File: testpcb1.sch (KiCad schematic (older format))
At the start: 42 parts

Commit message: pinout pro micro
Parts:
- added RV?: R_POT, symbol Device:R_POT
- added SW?: Rotary_Encoder, symbol Device:Rotary_Encoder
- added SW?: SW_Push, symbol Switch:SW_Push
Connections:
- net col0: now also U?.15 (14/PB3)
- net col1: now also U?.14 (16/PB2)
- net col2: now also U?.13 (10/PB6)
- net col3: now also U?.1 (TX0/PD3)
- net row0: now also U?.20 (A3/PF4)
- net row1: now also U?.19 (A2/PF5)
- net row2: now also U?.18 (A1/PF6)
- net row3: now also U?.17 (A0/PF7)
- net row4: now reaches U?.16 (15/PB1)
- net VCC: now reaches U?.21 (VCC)
- net RST: now reaches U?.22 (RST)
- net RST: now also SW?.1
- net GND: now reaches U?.23 (GND)
- net GND: now also SW?.2
- net POT: now reaches U?.7 (4/PD4)
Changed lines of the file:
@@
 Text GLabel 1150 1600 0    31   Input ~ 0
 SDL
+$Comp
+L Device:Rotary_Encoder SW?
+U 1 1 5F279AE0
+P 8850 1500
+F 0 "SW?" H 9080 1546 50  0000 L CNN
+F 1 "Rotary_Encoder" H 9080 1455 50  0000 L CNN
+F 2 "" H 8700 1660 50  0001 C CNN
+F 3 "~" H 8850 1760 50  0001 C CNN
+	1    8850 1500
+	1    0    0    -1
+$EndComp
+$Comp
+L Device:R_POT RV?
+U 1 1 5F27C616
+P 9000 4000
+F 0 "RV?" H 8931 4046 50  0000 R CNN
+F 1 "R_POT" H 8931 3955 50  0000 R CNN
+F 2 "" H 9000 4000 50  0001 C CNN
+F 3 "~" H 9000 4000 50  0001 C CNN
+	1    9000 4000
+	1    0    0    -1
+$EndComp
+Wire Wire Line
+	1300 1700 1150 1700
+Text GLabel 1150 1700 0    31   Input ~ 0
+POT
+Text GLabel 2850 1300 2    31   Input ~ 0
+RST
+Wire Wire Line
+	2700 1300 2850 1300
+Wire Wire Line
+	2700 1200 2850 1200
+Text GLabel 2850 1200 2    31   Input ~ 0
+GND
+$Comp
+L Switch:SW_Push SW?
+U 1 1 5F289AFB
+P 4200 1500
+F 0 "SW?" H 4200 1785 50  0000 C CNN
+F 1 "SW_Push" H 4200 1694 50  0000 C CNN
+F 2 "" H 4200 1700 50  0001 C CNN
+F 3 "~" H 4200 1700 50  0001 C CNN
+	1    4200 1500
+	1    0    0    -1
+$EndComp
+Wire Wire Line
+	4400 1500 4800 1500
+Wire Wire Line
+	4000 1500 3500 1500
+Text GLabel 3500 1500 0    31   Input ~ 0
+RST
+Text GLabel 4800 1500 2    31   Input ~ 0
+GND
+Text GLabel 2850 1400 2    31   Input ~ 0
+VCC
+Wire Wire Line
+	2850 1400 2700 1400
+Text GLabel 2850 1500 2    31   Input ~ 0
+row0
+Text GLabel 2850 1600 2    31   Input ~ 0
+row1
+Text GLabel 2850 1700 2    31   Input ~ 0
+row2
+Text GLabel 2850 1800 2    31   Input ~ 0
+row3
+Text GLabel 2850 1900 2    31   Input ~ 0
+row4
+Wire Wire Line
+	2850 1500 2700 1500
+Wire Wire Line
+	2700 1600 2850 1600
+Wire Wire Line
+	2850 1700 2700 1700
+Wire Wire Line
+	2700 1800 2850 1800
+Wire Wire Line
+	2850 1900 2700 1900
+Text GLabel 2850 2000 2    31   Input ~ 0
+col0
+Text GLabel 2850 2100 2    31   Input ~ 0
+col1
+Text GLabel 2850 2200 2    31   Input ~ 0
+col2
+Text GLabel 1150 1100 0    31   Input ~ 0
+col3
+Wire Wire Line
+	2850 2000 2700 2000
+Wire Wire Line
+	2700 2100 2850 2100
+Wire Wire Line
+	2850 2200 2700 2200
+Wire Wire Line
+	1300 1100 1150 1100
 $EndSCHEMATC

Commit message: vcc and gnd
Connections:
- net GND: no longer U?.23 (GND)
- net col3: now also U?.12 (9/PB5); no longer U?.1 (TX0/PD3)
- net ROT2: now reaches U?.2 (RX1/PD2)
- net VCC: no longer names the net of U?.21 (VCC)
- new net ROT1: U?.1 (TX0/PD3)
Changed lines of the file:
@@
 Wire Wire Line
 	2700 1200 2850 1200
-Text GLabel 2850 1200 2    31   Input ~ 0
-GND
 $Comp
 L Switch:SW_Push SW?
@@
 Text GLabel 4800 1500 2    31   Input ~ 0
 GND
-Text GLabel 2850 1400 2    31   Input ~ 0
-VCC
 Wire Wire Line
 	2850 1400 2700 1400
@@
 Text GLabel 2850 2200 2    31   Input ~ 0
 col2
-Text GLabel 1150 1100 0    31   Input ~ 0
+Text GLabel 1150 2200 0    31   Input ~ 0
 col3
 Wire Wire Line
@@
 	2850 2200 2700 2200
 Wire Wire Line
+	1300 2200 1150 2200
+Wire Wire Line
 	1300 1100 1150 1100
+Text GLabel 1150 1100 0    31   Input ~ 0
+ROT1
+Wire Wire Line
+	1300 1200 1150 1200
+Text GLabel 1150 1200 0    31   Input ~ 0
+ROT2
 $EndSCHEMATC

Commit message: power symbol library
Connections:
- net GND: now also U?.23 (GND)
- net VCC: now reaches U?.21 (VCC)
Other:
- moved on the sheet: SW?
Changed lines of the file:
@@
 Wire Wire Line
 	2700 1300 2850 1300
-Wire Wire Line
-	2700 1200 2850 1200
 $Comp
 L Switch:SW_Push SW?
 U 1 1 5F289AFB
-P 4200 1500
-F 0 "SW?" H 4200 1785 50  0000 C CNN
-F 1 "SW_Push" H 4200 1694 50  0000 C CNN
-F 2 "" H 4200 1700 50  0001 C CNN
-F 3 "~" H 4200 1700 50  0001 C CNN
-	1    4200 1500
+P 4050 1200
+F 0 "SW?" H 4050 1485 50  0000 C CNN
+F 1 "SW_Push" H 4050 1394 50  0000 C CNN
+F 2 "" H 4050 1400 50  0001 C CNN
+F 3 "~" H 4050 1400 50  0001 C CNN
+	1    4050 1200
 	1    0    0    -1
 $EndComp
-Wire Wire Line
-	4400 1500 4800 1500
-Wire Wire Line
-	4000 1500 3500 1500
-Text GLabel 3500 1500 0    31   Input ~ 0
+Text GLabel 3700 1200 0    31   Input ~ 0
 RST
-Text GLabel 4800 1500 2    31   Input ~ 0
-GND
-Wire Wire Line
-	2850 1400 2700 1400
 Text GLabel 2850 1500 2    31   Input ~ 0
 row0
@@
 Text GLabel 1150 1200 0    31   Input ~ 0
 ROT2
+$Comp
+L power:GND #PWR?
+U 1 1 5F27AF68
+P 2800 1200
+F 0 "#PWR?" H 2800 950 50  0001 C CNN
+F 1 "GND" V 2805 1072 50  0000 R CNN
+F 2 "" H 2800 1200 50  0001 C CNN
+F 3 "" H 2800 1200 50  0001 C CNN
+	1    2800 1200
+	0    -1   -1   0
+$EndComp
+$Comp
+L power:VCC #PWR?
+U 1 1 5F27BB79
+P 2800 1400
+F 0 "#PWR?" H 2800 1250 50  0001 C CNN
+F 1 "VCC" V 2815 1528 50  0000 L CNN
+F 2 "" H 2800 1400 50  0001 C CNN
+F 3 "" H 2800 1400 50  0001 C CNN
+	1    2800 1400
+	0    1    1    0
+$EndComp
+Wire Wire Line
+	2800 1200 2700 1200
+Wire Wire Line
+	2700 1400 2800 1400
+$Comp
+L power:GND #PWR?
+U 1 1 5F2859D6
+P 4400 1200
+F 0 "#PWR?" H 4400 950 50  0001 C CNN
+F 1 "GND" V 4405 1072 50  0000 R CNN
+F 2 "" H 4400 1200 50  0001 C CNN
+F 3 "" H 4400 1200 50  0001 C CNN
+	1    4400 1200
+	0    -1   -1   0
+$EndComp
+Wire Wire Line
+	3850 1200 3700 1200
+Wire Wire Line
+	4400 1200 4250 1200
 $EndSCHEMATC

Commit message: OLED
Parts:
- added J?: Conn_01x04_Female, symbol Connector:Conn_01x04_Female
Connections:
- net GND: now also U?.3 (GND), U?.4 (GND), J?.4 (Pin_4)
- net SDA: now also J?.1 (Pin_1)
- net VCC: now also J?.3 (Pin_3)
- net SDL renamed SCL
- net SCL: now also J?.2 (Pin_2)
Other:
- moved on the sheet: RV?, SW?
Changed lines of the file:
@@
 SDA
 Text GLabel 1150 1600 0    31   Input ~ 0
-SDL
+SCL
 $Comp
 L Device:Rotary_Encoder SW?
 U 1 1 5F279AE0
-P 8850 1500
-F 0 "SW?" H 9080 1546 50  0000 L CNN
-F 1 "Rotary_Encoder" H 9080 1455 50  0000 L CNN
-F 2 "" H 8700 1660 50  0001 C CNN
-F 3 "~" H 8850 1760 50  0001 C CNN
-	1    8850 1500
+P 1750 4750
+F 0 "SW?" H 1980 4796 50  0000 L CNN
+F 1 "Rotary_Encoder" H 1980 4705 50  0000 L CNN
+F 2 "" H 1600 4910 50  0001 C CNN
+F 3 "~" H 1750 5010 50  0001 C CNN
+	1    1750 4750
 	1    0    0    -1
 $EndComp
@@
 L Device:R_POT RV?
 U 1 1 5F27C616
-P 9000 4000
-F 0 "RV?" H 8931 4046 50  0000 R CNN
-F 1 "R_POT" H 8931 3955 50  0000 R CNN
-F 2 "" H 9000 4000 50  0001 C CNN
-F 3 "~" H 9000 4000 50  0001 C CNN
-	1    9000 4000
+P 1750 5850
+F 0 "RV?" H 1681 5896 50  0000 R CNN
+F 1 "R_POT" H 1681 5805 50  0000 R CNN
+F 2 "" H 1750 5850 50  0001 C CNN
+F 3 "~" H 1750 5850 50  0001 C CNN
+	1    1750 5850
 	1    0    0    -1
 $EndComp
@@
 Wire Wire Line
 	4400 1200 4250 1200
+$Comp
+L Connector:Conn_01x04_Female J?
+U 1 1 5F2A1EA2
+P 1700 6600
+F 0 "J?" H 1728 6576 50  0000 L CNN
+F 1 "Conn_01x04_Female" H 1728 6485 50  0000 L CNN
+F 2 "" H 1700 6600 50  0001 C CNN
+F 3 "~" H 1700 6600 50  0001 C CNN
+	1    1700 6600
+	1    0    0    -1
+$EndComp
+Text GLabel 1350 6600 0    50   Input ~ 0
+SCL
+Text GLabel 1350 6500 0    50   Input ~ 0
+SDA
+Wire Wire Line
+	1350 6500 1500 6500
+Wire Wire Line
+	1350 6600 1500 6600
+$Comp
+L power:GND #PWR?
+U 1 1 5F2B8AC8
+P 1400 6800
+F 0 "#PWR?" H 1400 6550 50  0001 C CNN
+F 1 "GND" V 1405 6672 50  0000 R CNN
+F 2 "" H 1400 6800 50  0001 C CNN
+F 3 "" H 1400 6800 50  0001 C CNN
+	1    1400 6800
+	0    1    1    0
+$EndComp
+$Comp
+L power:VCC #PWR?
+U 1 1 5F2B9324
+P 1400 6700
+F 0 "#PWR?" H 1400 6550 50  0001 C CNN
+F 1 "VCC" V 1415 6827 50  0000 L CNN
+F 2 "" H 1400 6700 50  0001 C CNN
+F 3 "" H 1400 6700 50  0001 C CNN
+	1    1400 6700
+	0    -1   -1   0
+$EndComp
+Wire Wire Line
+	1400 6700 1500 6700
+Wire Wire Line
+	1500 6800 1400 6800
+$Comp
+L power:GND #PWR?
+U 1 1 5F2BFDF9
+P 1150 1300
+F 0 "#PWR?" H 1150 1050 50  0001 C CNN
+F 1 "GND" V 1155 1172 50  0000 R CNN
+F 2 "" H 1150 1300 50  0001 C CNN
+F 3 "" H 1150 1300 50  0001 C CNN
+	1    1150 1300
+	0    1    1    0
+$EndComp
+Wire Wire Line
+	1300 1300 1200 1300
+Wire Wire Line
+	1300 1400 1200 1400
+Wire Wire Line
+	1200 1400 1200 1300
+Connection ~ 1200 1300
+Wire Wire Line
+	1200 1300 1150 1300
 $EndSCHEMATC

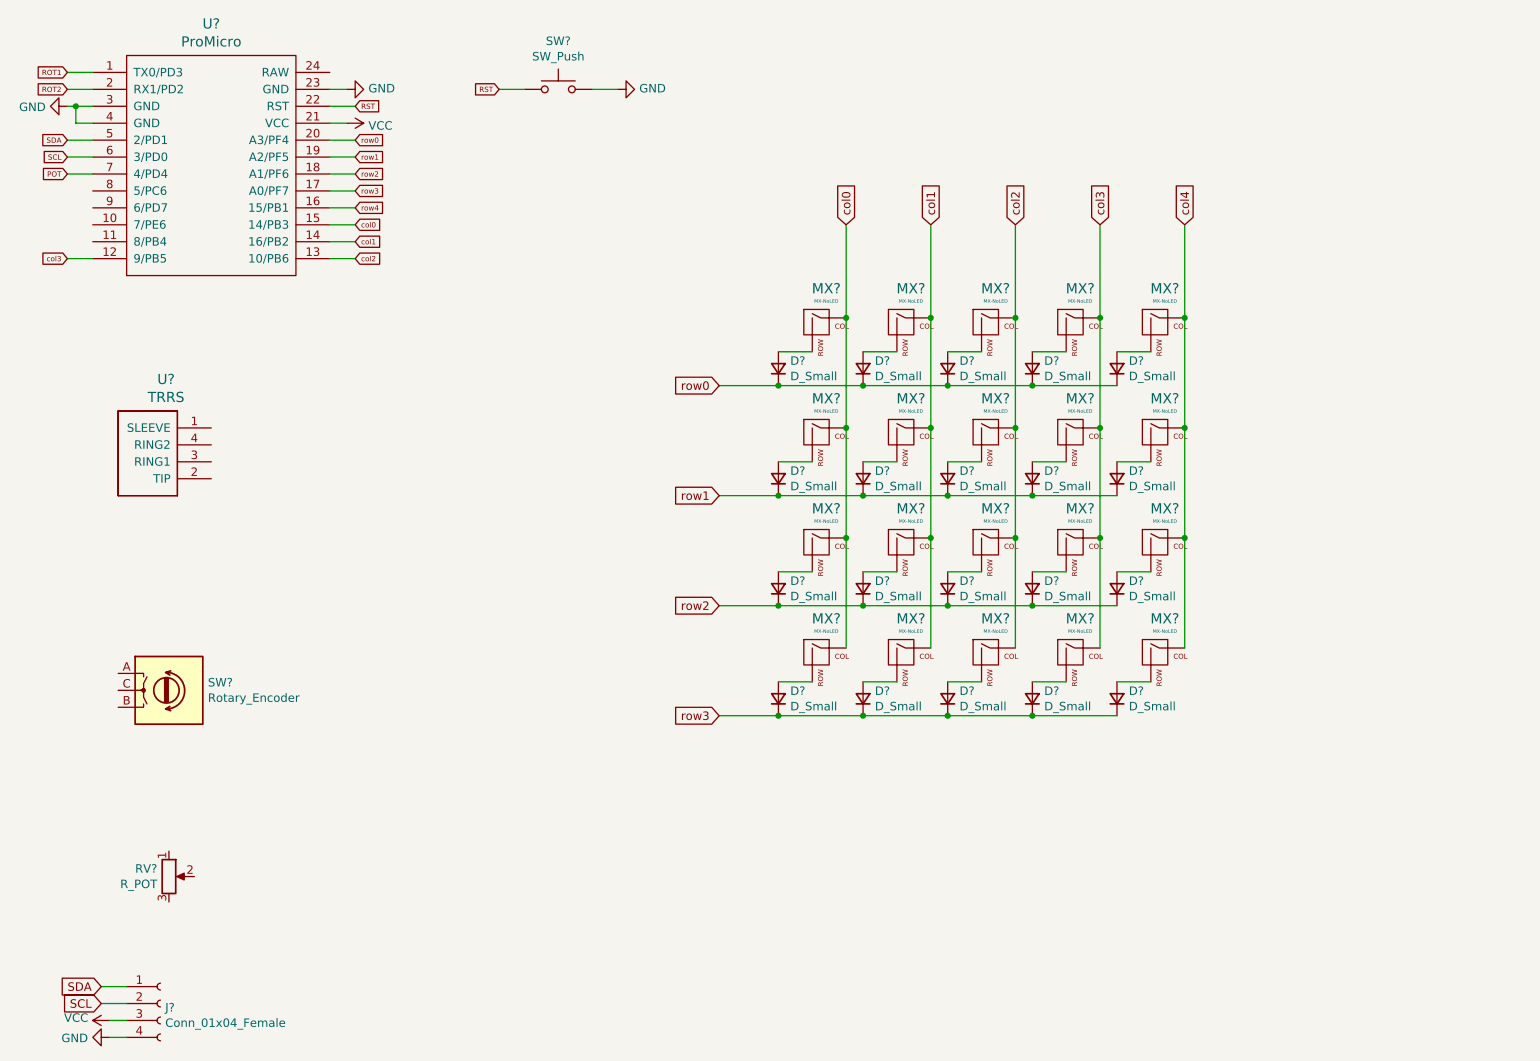
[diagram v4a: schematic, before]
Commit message: wired rotary encoder switch
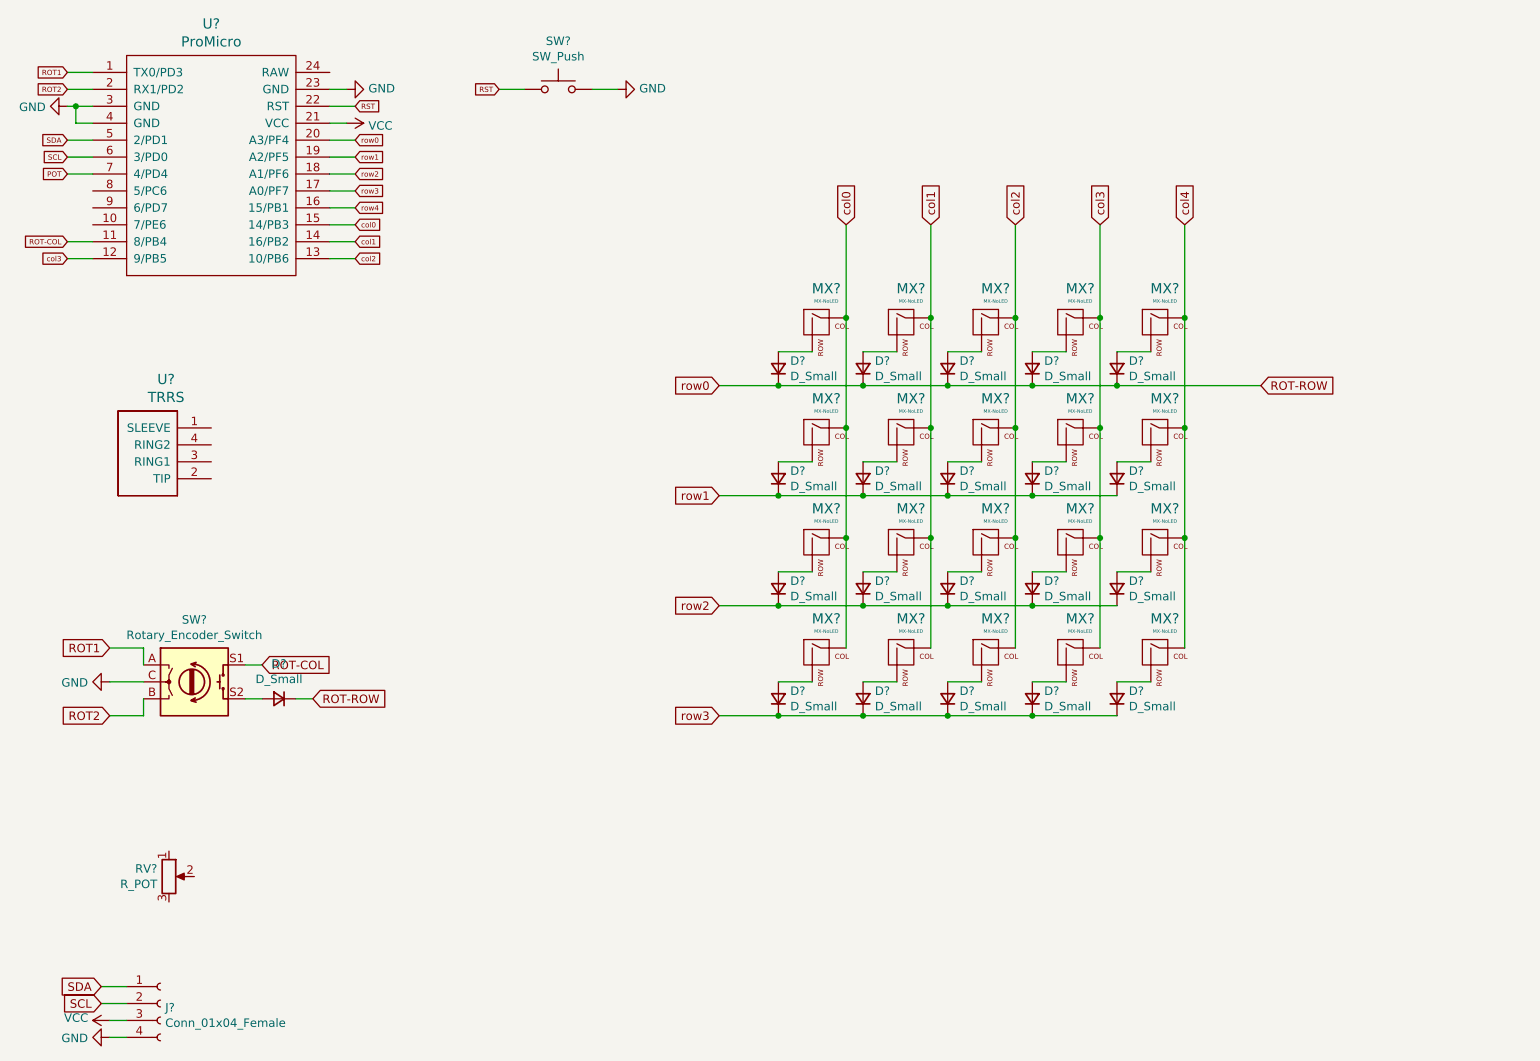
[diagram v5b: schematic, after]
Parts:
- removed SW?: Rotary_Encoder, symbol Device:Rotary_Encoder
- added D?: D_Small, symbol Device:D_Small
- added SW?: Rotary_Encoder_Switch, symbol Device:Rotary_Encoder_Switch
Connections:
- net GND: now also SW?.C
- net ROT1: now also SW?.A
- net ROT2: now also SW?.B
- net ROT-COL: now reaches U?.11 (8/PB4)
- net ROT-COL: now also SW?.S1
- net row0 renamed ROT-ROW
- net ROT-ROW: now also D?.1 (K)
- new net: D?.2 (A), SW?.S2
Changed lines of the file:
@@
 SCL
-$Comp
-L Device:Rotary_Encoder SW?
-U 1 1 5F279AE0
-P 1750 4750
-F 0 "SW?" H 1980 4796 50  0000 L CNN
-F 1 "Rotary_Encoder" H 1980 4705 50  0000 L CNN
-F 2 "" H 1600 4910 50  0001 C CNN
-F 3 "~" H 1750 5010 50  0001 C CNN
-	1    1750 4750
-	1    0    0    -1
-$EndComp
 $Comp
 L Device:R_POT RV?
@@
 Wire Wire Line
 	1200 1300 1150 1300
+$Comp
+L Device:Rotary_Encoder_Switch SW?
+U 1 1 5F2D27A0
+P 1900 4700
+F 0 "SW?" H 1900 5067 50  0000 C CNN
+F 1 "Rotary_Encoder_Switch" H 1900 4976 50  0000 C CNN
+F 2 "" H 1750 4860 50  0001 C CNN
+F 3 "~" H 1900 4960 50  0001 C CNN
+	1    1900 4700
+	1    0    0    -1
+$EndComp
+Wire Wire Line
+	7350 2950 8200 2950
+Connection ~ 7350 2950
+Text GLabel 8200 2950 2    50   Input ~ 0
+ROT-ROW
+Text GLabel 1150 2100 0    31   Input ~ 0
+ROT-COL
+Wire Wire Line
+	1150 2100 1300 2100
+$Comp
+L Device:D_Small D?
+U 1 1 5F2DBE74
+P 2400 4800
+F 0 "D?" H 2400 4593 50  0000 C CNN
+F 1 "D_Small" H 2400 4684 50  0000 C CNN
+F 2 "" V 2400 4800 50  0001 C CNN
+F 3 "~" V 2400 4800 50  0001 C CNN
+	1    2400 4800
+	-1   0    0    1
+$EndComp
+Wire Wire Line
+	2300 4800 2200 4800
+Wire Wire Line
+	2500 4800 2600 4800
+Text GLabel 2600 4800 2    50   Input ~ 0
+ROT-ROW
+Text GLabel 2300 4600 2    50   Input ~ 0
+ROT-COL
+Wire Wire Line
+	2300 4600 2200 4600
+$Comp
+L power:GND #PWR?
+U 1 1 5F318747
+P 1400 4700
+F 0 "#PWR?" H 1400 4450 50  0001 C CNN
+F 1 "GND" V 1405 4572 50  0000 R CNN
+F 2 "" H 1400 4700 50  0001 C CNN
+F 3 "" H 1400 4700 50  0001 C CNN
+	1    1400 4700
+	0    1    1    0
+$EndComp
+Wire Wire Line
+	1600 4700 1400 4700
+Text GLabel 1400 4500 0    50   Input ~ 0
+ROT1
+Text GLabel 1400 4900 0    50   Input ~ 0
+ROT2
+Wire Wire Line
+	1600 4600 1600 4500
+Wire Wire Line
+	1600 4500 1400 4500
+Wire Wire Line
+	1600 4800 1600 4900
+Wire Wire Line
+	1600 4900 1400 4900
 $EndSCHEMATC

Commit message: potentiometer
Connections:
- net GND: now also RV?.3
- net VCC: now also RV?.1
- net ANALOG: now reaches RV?.2
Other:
- moved on the sheet: D?, RV?, SW?
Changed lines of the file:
@@
 L Device:R_POT RV?
 U 1 1 5F27C616
-P 1750 5850
-F 0 "RV?" H 1681 5896 50  0000 R CNN
-F 1 "R_POT" H 1681 5805 50  0000 R CNN
-F 2 "" H 1750 5850 50  0001 C CNN
-F 3 "~" H 1750 5850 50  0001 C CNN
-	1    1750 5850
+P 2000 5650
+F 0 "RV?" H 1931 5696 50  0000 R CNN
+F 1 "R_POT" H 1931 5605 50  0000 R CNN
+F 2 "" H 2000 5650 50  0001 C CNN
+F 3 "~" H 2000 5650 50  0001 C CNN
+	1    2000 5650
 	1    0    0    -1
 $EndComp
@@
 L Device:Rotary_Encoder_Switch SW?
 U 1 1 5F2D27A0
-P 1900 4700
-F 0 "SW?" H 1900 5067 50  0000 C CNN
-F 1 "Rotary_Encoder_Switch" H 1900 4976 50  0000 C CNN
-F 2 "" H 1750 4860 50  0001 C CNN
-F 3 "~" H 1900 4960 50  0001 C CNN
-	1    1900 4700
+P 2000 4750
+F 0 "SW?" H 2000 5117 50  0000 C CNN
+F 1 "Rotary_Encoder_Switch" H 2000 5026 50  0000 C CNN
+F 2 "" H 1850 4910 50  0001 C CNN
+F 3 "~" H 2000 5010 50  0001 C CNN
+	1    2000 4750
 	1    0    0    -1
 $EndComp
@@
 L Device:D_Small D?
 U 1 1 5F2DBE74
-P 2400 4800
-F 0 "D?" H 2400 4593 50  0000 C CNN
-F 1 "D_Small" H 2400 4684 50  0000 C CNN
-F 2 "" V 2400 4800 50  0001 C CNN
-F 3 "~" V 2400 4800 50  0001 C CNN
-	1    2400 4800
+P 2500 5000
+F 0 "D?" H 2500 4793 50  0000 C CNN
+F 1 "D_Small" H 2500 4884 50  0000 C CNN
+F 2 "" V 2500 5000 50  0001 C CNN
+F 3 "~" V 2500 5000 50  0001 C CNN
+	1    2500 5000
 	-1   0    0    1
 $EndComp
 Wire Wire Line
-	2300 4800 2200 4800
-Wire Wire Line
-	2500 4800 2600 4800
-Text GLabel 2600 4800 2    50   Input ~ 0
+	2600 5000 2700 5000
+Text GLabel 2700 5000 2    50   Input ~ 0
 ROT-ROW
-Text GLabel 2300 4600 2    50   Input ~ 0
+Text GLabel 2400 4650 2    50   Input ~ 0
 ROT-COL
 Wire Wire Line
-	2300 4600 2200 4600
+	2400 4650 2300 4650
 $Comp
 L power:GND #PWR?
 U 1 1 5F318747
-P 1400 4700
-F 0 "#PWR?" H 1400 4450 50  0001 C CNN
-F 1 "GND" V 1405 4572 50  0000 R CNN
-F 2 "" H 1400 4700 50  0001 C CNN
-F 3 "" H 1400 4700 50  0001 C CNN
-	1    1400 4700
-	0    1    1    0
-$EndComp
-Wire Wire Line
-	1600 4700 1400 4700
-Text GLabel 1400 4500 0    50   Input ~ 0
+P 1500 4750
+F 0 "#PWR?" H 1500 4500 50  0001 C CNN
+F 1 "GND" V 1505 4622 50  0000 R CNN
+F 2 "" H 1500 4750 50  0001 C CNN
+F 3 "" H 1500 4750 50  0001 C CNN
+	1    1500 4750
+	0    1    1    0
+$EndComp
+Wire Wire Line
+	1700 4750 1500 4750
+Text GLabel 1500 4550 0    50   Input ~ 0
 ROT1
-Text GLabel 1400 4900 0    50   Input ~ 0
+Text GLabel 1500 4950 0    50   Input ~ 0
 ROT2
 Wire Wire Line
-	1600 4600 1600 4500
-Wire Wire Line
-	1600 4500 1400 4500
-Wire Wire Line
-	1600 4800 1600 4900
-Wire Wire Line
-	1600 4900 1400 4900
+	1700 4650 1700 4550
+Wire Wire Line
+	1700 4550 1500 4550
+Wire Wire Line
+	1700 4850 1700 4950
+Wire Wire Line
+	1700 4950 1500 4950
+Wire Wire Line
+	2300 4850 2300 5000
+Wire Wire Line
+	2300 5000 2400 5000
+Wire Wire Line
+	2150 5650 2250 5650
+Text GLabel 2250 5650 2    50   Input ~ 0
+ANALOG
+Wire Wire Line
+	2000 5500 2000 5400
+Wire Wire Line
+	2000 5800 2000 5900
+Text GLabel 2000 5400 1    50   Input ~ 0
+VCC
+Text GLabel 2000 5900 3    50   Input ~ 0
+GND
 $EndSCHEMATC
